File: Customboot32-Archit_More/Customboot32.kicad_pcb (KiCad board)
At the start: 2 copper layers, 7 parts, among them Q1 SS8050, Q2 SS8050, U1 ESP32-WROOM-32D, U2 STM32F103C8T6, U3 AMS1117-3.3, U4 CP2102N-Axx-xQFN28

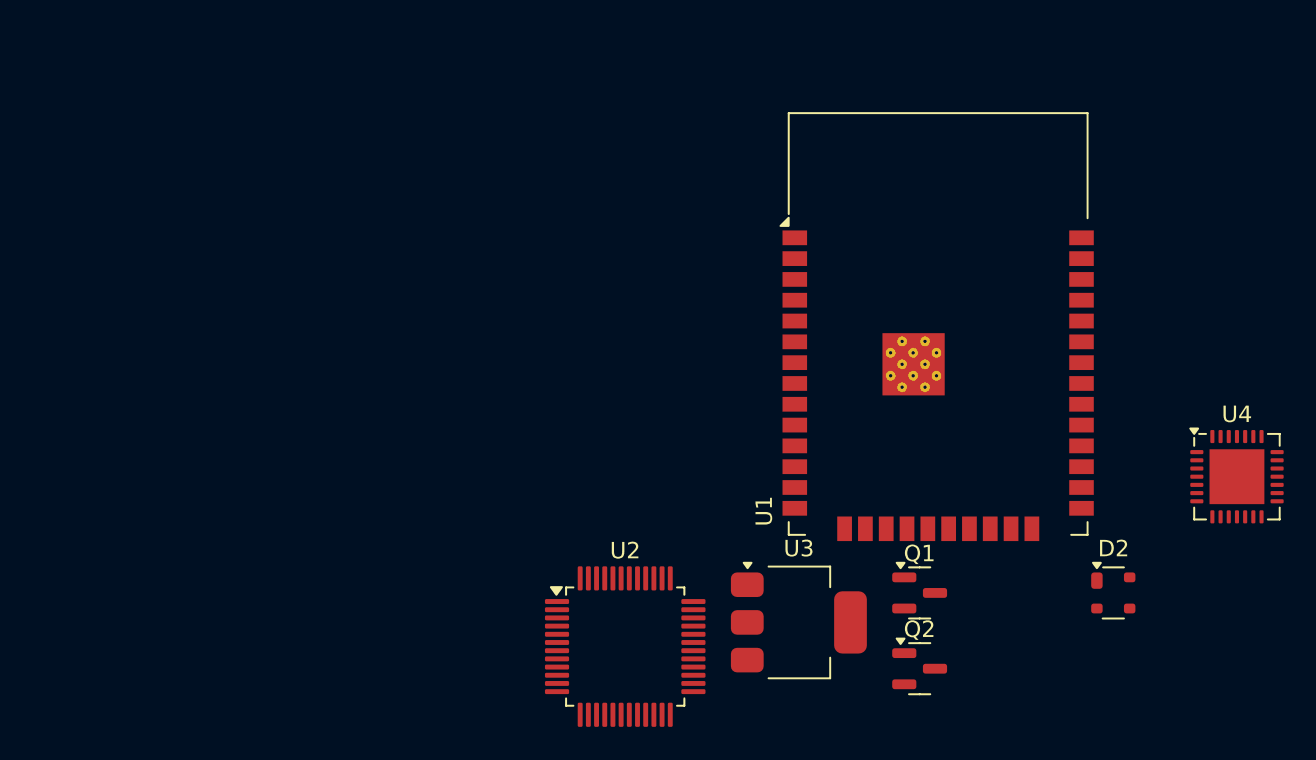
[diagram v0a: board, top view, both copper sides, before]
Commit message: ESP OTA code added
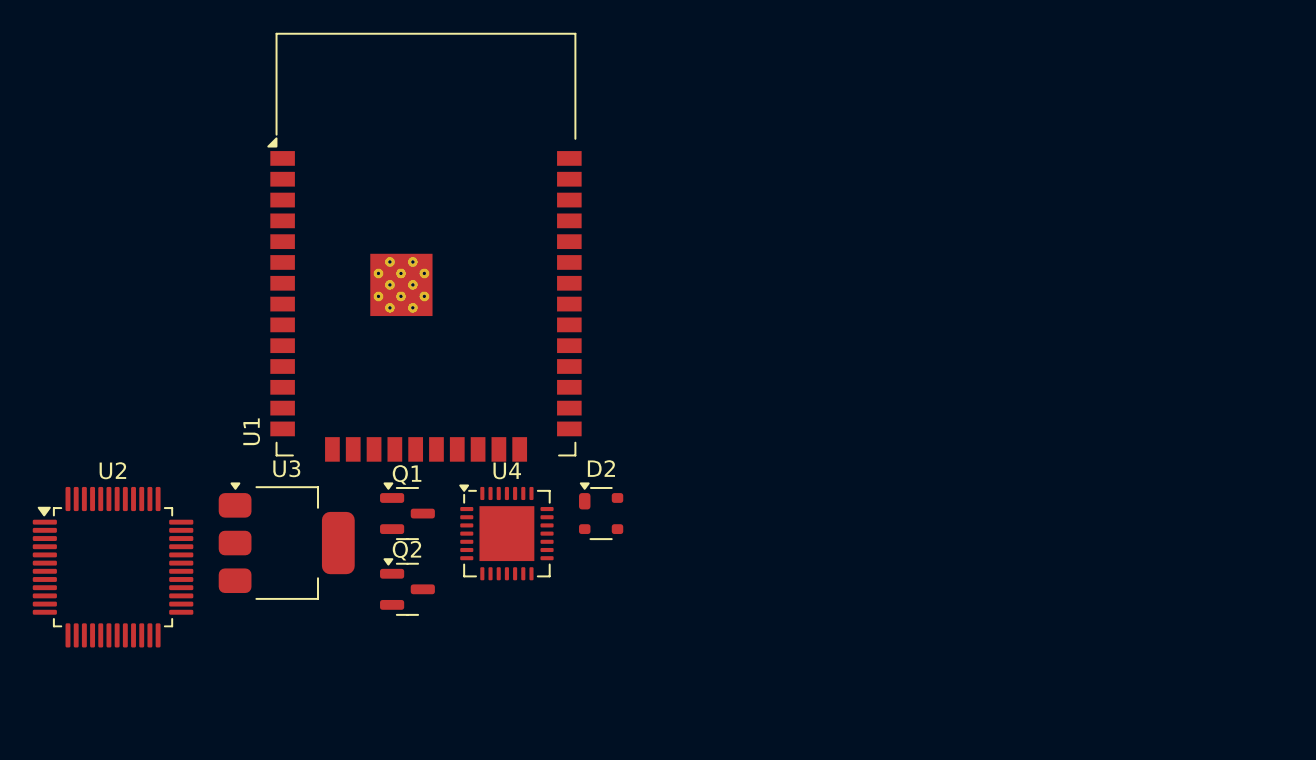
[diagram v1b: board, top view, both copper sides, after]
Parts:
- moved U4 44.7 mm to (105.0, 75.2)
- moved U3 31.6 mm to (91.6, 75.8)
- moved U1 31.6 mm to (100.1, 60.6)
- moved Q1 31.6 mm to (98.9, 74.0)
- moved Q2 31.6 mm to (98.9, 78.6)
- moved U2 31.6 mm to (81.0, 77.3)
- moved D2 31.6 mm to (110.8, 74.0)
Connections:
- net +3.3V renamed VBAT
- net /HSE_IN renamed PD0
- net /HSE_OUT renamed PD1
- net /RXD2 renamed IO16
- net /TXD2 renamed TXD2
- net /UART1_TX renamed PA9
- net GND renamed VSS
- net Net-(U2-BOOT0) renamed BOOT0
- net Net-(U2-NRST) renamed NRST
- U1 pad 10: unconnected-(U1-IO25-Pad10) -> IO25
- U1 pad 11: unconnected-(U1-IO26-Pad11) -> IO26
- U1 pad 12: unconnected-(U1-IO27-Pad12) -> IO27
- U1 pad 13: unconnected-(U1-IO14-Pad13) -> IO14
- U1 pad 14: unconnected-(U1-IO12-Pad14) -> IO12
- U1 pad 16: unconnected-(U1-IO13-Pad16) -> IO13
- U1 pad 17: unconnected-(U1-SHD/SD2-Pad17) -> SD2
- U1 pad 18: unconnected-(U1-SWP/SD3-Pad18) -> SD3
- U1 pad 19: unconnected-(U1-SCS/CMD-Pad19) -> CMD
- U1 pad 20: unconnected-(U1-SCK/CLK-Pad20) -> CLK
- U1 pad 21: unconnected-(U1-SDO/SD0-Pad21) -> SD0
- U1 pad 22: unconnected-(U1-SDI/SD1-Pad22) -> SD1
- U1 pad 23: unconnected-(U1-IO15-Pad23) -> IO15
- U1 pad 24: unconnected-(U1-IO2-Pad24) -> IO2
- U1 pad 26: unconnected-(U1-IO4-Pad26) -> IO4
- U1 pad 29: unconnected-(U1-IO5-Pad29) -> IO5
- U1 pad 30: unconnected-(U1-IO18-Pad30) -> IO18
- U1 pad 33: unconnected-(U1-IO21-Pad33) -> IO21
- U1 pad 36: unconnected-(U1-IO22-Pad36) -> IO22
- U1 pad 37: unconnected-(U1-IO23-Pad37) -> IO23
- U1 pad 4: unconnected-(U1-SENSOR_VP-Pad4) -> SENSOR_VP
- U1 pad 5: unconnected-(U1-SENSOR_VN-Pad5) -> SENSOR_VN
- U1 pad 6: unconnected-(U1-IO34-Pad6) -> IO34
- U1 pad 7: unconnected-(U1-IO35-Pad7) -> IO35
- U1 pad 8: unconnected-(U1-IO32-Pad8) -> IO32
- U1 pad 9: unconnected-(U1-IO33-Pad9) -> IO33
- U2 pad 10: unconnected-(U2-PA0-Pad10) -> PA0
- U2 pad 11: unconnected-(U2-PA1-Pad11) -> PA1
- U2 pad 12: unconnected-(U2-PA2-Pad12) -> PA2
- U2 pad 13: unconnected-(U2-PA3-Pad13) -> PA3
- U2 pad 14: unconnected-(U2-PA4-Pad14) -> PA4
- U2 pad 15: unconnected-(U2-PA5-Pad15) -> PA5
- U2 pad 16: unconnected-(U2-PA6-Pad16) -> PA6
- U2 pad 17: unconnected-(U2-PA7-Pad17) -> PA7
- U2 pad 18: unconnected-(U2-PB0-Pad18) -> PB0
- U2 pad 19: unconnected-(U2-PB1-Pad19) -> PB1
- U2 pad 2: unconnected-(U2-PC13-Pad2) -> PC13
- U2 pad 20: unconnected-(U2-PB2-Pad20) -> PB2
- U2 pad 21: unconnected-(U2-PB10-Pad21) -> PB10
- U2 pad 22: unconnected-(U2-PB11-Pad22) -> PB11
- U2 pad 25: unconnected-(U2-PB12-Pad25) -> PB12
- U2 pad 26: unconnected-(U2-PB13-Pad26) -> PB13
- U2 pad 27: unconnected-(U2-PB14-Pad27) -> PB14
- U2 pad 28: unconnected-(U2-PB15-Pad28) -> PB15
- U2 pad 29: unconnected-(U2-PA8-Pad29) -> PA8
- U2 pad 3: unconnected-(U2-PC14-Pad3) -> PC14
- U2 pad 32: unconnected-(U2-PA11-Pad32) -> PA11
- U2 pad 34: unconnected-(U2-PA13-Pad34) -> PA13
- U2 pad 37: unconnected-(U2-PA14-Pad37) -> PA14
- U2 pad 38: unconnected-(U2-PA15-Pad38) -> PA15
- U2 pad 39: unconnected-(U2-PB3-Pad39) -> PB3
- U2 pad 4: unconnected-(U2-PC15-Pad4) -> PC15
- U2 pad 40: unconnected-(U2-PB4-Pad40) -> PB4
- U2 pad 41: unconnected-(U2-PB5-Pad41) -> PB5
- U2 pad 42: unconnected-(U2-PB6-Pad42) -> PB6
- U2 pad 43: unconnected-(U2-PB7-Pad43) -> PB7
- U2 pad 45: unconnected-(U2-PB8-Pad45) -> PB8
- U2 pad 46: unconnected-(U2-PB9-Pad46) -> PB9
- U2 pad 9: unconnected-(U2-VDDA-Pad9) -> VDDA
